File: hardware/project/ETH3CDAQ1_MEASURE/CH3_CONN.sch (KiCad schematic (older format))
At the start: 1 part, among them J1301 Conn_02x10_Odd_Even

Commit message: PCB layout
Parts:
- renumbered J1301 to J1001
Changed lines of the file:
@@
 AR Path="/5FDF6197/5FF0E84A" Ref="J?"  Part="1"
 AR Path="/5FE2FF08/5FF0E84A" Ref="J?"  Part="1"
-AR Path="/5FF09887/5FF0E84A" Ref="J1301"  Part="1"
-F 0 "J1301" H 5450 3667 50  0000 C CNN
+AR Path="/5FF09887/5FF0E84A" Ref="J1001"  Part="1"
+F 0 "J1001" H 5450 3667 50  0000 C CNN
 F 1 "Conn_02x10_Odd_Even" H 5450 3576 50  0000 C CNN
 F 2 "Connector_PinSocket_2.54mm:PinSocket_2x10_P2.54mm_Vertical" H 5400 3050 50  0001 C CNN
@@
 AR Path="/5FDF6197/5FF0E850" Ref="#PWR?"  Part="1"
 AR Path="/5FE2FF08/5FF0E850" Ref="#PWR?"  Part="1"
-AR Path="/5FF09887/5FF0E850" Ref="#PWR01302"  Part="1"
-F 0 "#PWR01302" H 5200 2500 50  0001 C CNN
+AR Path="/5FF09887/5FF0E850" Ref="#PWR01002"  Part="1"
+F 0 "#PWR01002" H 5200 2500 50  0001 C CNN
 F 1 "GND" V 5200 2600 50  0000 R CNN
 F 2 "" H 5200 2750 50  0001 C CNN
@@
 AR Path="/5FDF6197/5FF0E856" Ref="#PWR?"  Part="1"
 AR Path="/5FE2FF08/5FF0E856" Ref="#PWR?"  Part="1"
-AR Path="/5FF09887/5FF0E856" Ref="#PWR01303"  Part="1"
-F 0 "#PWR01303" H 5200 2600 50  0001 C CNN
+AR Path="/5FF09887/5FF0E856" Ref="#PWR01003"  Part="1"
+F 0 "#PWR01003" H 5200 2600 50  0001 C CNN
 F 1 "GND" V 5200 2700 50  0000 R CNN
 F 2 "" H 5200 2850 50  0001 C CNN
@@
 AR Path="/5FDF6197/5FF0E85C" Ref="#PWR?"  Part="1"
 AR Path="/5FE2FF08/5FF0E85C" Ref="#PWR?"  Part="1"
-AR Path="/5FF09887/5FF0E85C" Ref="#PWR01308"  Part="1"
-F 0 "#PWR01308" H 5700 2600 50  0001 C CNN
+AR Path="/5FF09887/5FF0E85C" Ref="#PWR01008"  Part="1"
+F 0 "#PWR01008" H 5700 2600 50  0001 C CNN
 F 1 "GND" V 5700 2700 50  0000 R CNN
 F 2 "" H 5700 2850 50  0001 C CNN
@@
 AR Path="/5FDF6197/5FF0E862" Ref="#PWR?"  Part="1"
 AR Path="/5FE2FF08/5FF0E862" Ref="#PWR?"  Part="1"
-AR Path="/5FF09887/5FF0E862" Ref="#PWR01301"  Part="1"
-F 0 "#PWR01301" H 5200 2400 50  0001 C CNN
+AR Path="/5FF09887/5FF0E862" Ref="#PWR01001"  Part="1"
+F 0 "#PWR01001" H 5200 2400 50  0001 C CNN
 F 1 "GND" V 5200 2500 50  0000 R CNN
 F 2 "" H 5200 2650 50  0001 C CNN
@@
 AR Path="/5FDF6197/5FF0E87C" Ref="#PWR?"  Part="1"
 AR Path="/5FE2FF08/5FF0E87C" Ref="#PWR?"  Part="1"
-AR Path="/5FF09887/5FF0E87C" Ref="#PWR01304"  Part="1"
-F 0 "#PWR01304" H 5200 3000 50  0001 C CNN
+AR Path="/5FF09887/5FF0E87C" Ref="#PWR01004"  Part="1"
+F 0 "#PWR01004" H 5200 3000 50  0001 C CNN
 F 1 "GND" V 5200 3100 50  0000 R CNN
 F 2 "" H 5200 3250 50  0001 C CNN
@@
 AR Path="/5FDF6197/5FF0E882" Ref="#PWR?"  Part="1"
 AR Path="/5FE2FF08/5FF0E882" Ref="#PWR?"  Part="1"
-AR Path="/5FF09887/5FF0E882" Ref="#PWR01309"  Part="1"
-F 0 "#PWR01309" H 5700 3000 50  0001 C CNN
+AR Path="/5FF09887/5FF0E882" Ref="#PWR01009"  Part="1"
+F 0 "#PWR01009" H 5700 3000 50  0001 C CNN
 F 1 "GND" V 5700 3100 50  0000 R CNN
 F 2 "" H 5700 3250 50  0001 C CNN
@@
 AR Path="/5FDF6197/5FF0E888" Ref="#PWR?"  Part="1"
 AR Path="/5FE2FF08/5FF0E888" Ref="#PWR?"  Part="1"
-AR Path="/5FF09887/5FF0E888" Ref="#PWR01305"  Part="1"
-F 0 "#PWR01305" H 5200 3200 50  0001 C CNN
+AR Path="/5FF09887/5FF0E888" Ref="#PWR01005"  Part="1"
+F 0 "#PWR01005" H 5200 3200 50  0001 C CNN
 F 1 "+3.3V" V 5200 3500 50  0000 L CNN
 F 2 "" H 5200 3350 50  0001 C CNN
@@
 AR Path="/5FDF6197/5FF0E88E" Ref="#PWR?"  Part="1"
 AR Path="/5FE2FF08/5FF0E88E" Ref="#PWR?"  Part="1"
-AR Path="/5FF09887/5FF0E88E" Ref="#PWR01310"  Part="1"
-F 0 "#PWR01310" H 5700 3200 50  0001 C CNN
+AR Path="/5FF09887/5FF0E88E" Ref="#PWR01010"  Part="1"
+F 0 "#PWR01010" H 5700 3200 50  0001 C CNN
 F 1 "+3.3V" V 5700 3500 50  0000 L CNN
 F 2 "" H 5700 3350 50  0001 C CNN
@@
 AR Path="/5FDF6197/5FF0E894" Ref="#PWR?"  Part="1"
 AR Path="/5FE2FF08/5FF0E894" Ref="#PWR?"  Part="1"
-AR Path="/5FF09887/5FF0E894" Ref="#PWR01306"  Part="1"
-F 0 "#PWR01306" H 5200 3300 50  0001 C CNN
+AR Path="/5FF09887/5FF0E894" Ref="#PWR01006"  Part="1"
+F 0 "#PWR01006" H 5200 3300 50  0001 C CNN
 F 1 "+9V" V 5200 3600 50  0000 L CNN
 F 2 "" H 5200 3450 50  0001 C CNN
@@
 AR Path="/5FDF6197/5FF0E89A" Ref="#PWR?"  Part="1"
 AR Path="/5FE2FF08/5FF0E89A" Ref="#PWR?"  Part="1"
-AR Path="/5FF09887/5FF0E89A" Ref="#PWR01311"  Part="1"
-F 0 "#PWR01311" H 5700 3300 50  0001 C CNN
+AR Path="/5FF09887/5FF0E89A" Ref="#PWR01011"  Part="1"
+F 0 "#PWR01011" H 5700 3300 50  0001 C CNN
 F 1 "+5V" V 5700 3600 50  0000 L CNN
 F 2 "" H 5700 3450 50  0001 C CNN
@@
 AR Path="/5FDF6197/5FF0E8A0" Ref="#PWR?"  Part="1"
 AR Path="/5FE2FF08/5FF0E8A0" Ref="#PWR?"  Part="1"
-AR Path="/5FF09887/5FF0E8A0" Ref="#PWR01307"  Part="1"
-F 0 "#PWR01307" H 5200 3400 50  0001 C CNN
+AR Path="/5FF09887/5FF0E8A0" Ref="#PWR01007"  Part="1"
+F 0 "#PWR01007" H 5200 3400 50  0001 C CNN
 F 1 "-18V" V 5200 3700 50  0000 L CNN
 F 2 "" H 5200 3550 50  0001 C CNN
@@
 AR Path="/5FDF6197/5FF0E8A6" Ref="#PWR?"  Part="1"
 AR Path="/5FE2FF08/5FF0E8A6" Ref="#PWR?"  Part="1"
-AR Path="/5FF09887/5FF0E8A6" Ref="#PWR01312"  Part="1"
-F 0 "#PWR01312" H 5700 3400 50  0001 C CNN
+AR Path="/5FF09887/5FF0E8A6" Ref="#PWR01012"  Part="1"
+F 0 "#PWR01012" H 5700 3400 50  0001 C CNN
 F 1 "+18V" V 5700 3700 50  0000 L CNN
 F 2 "" H 5700 3550 50  0001 C CNN

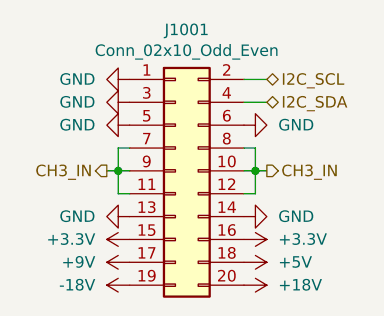
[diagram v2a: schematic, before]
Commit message: Started development of first current measurement module. Added CAN to the DAQ module.
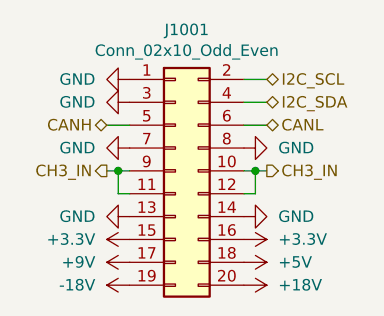
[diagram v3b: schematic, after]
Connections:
- net CH3_IN: no longer J1001.7 (Pin_7), J1001.8 (Pin_8)
- net GND: now also J1001.7 (Pin_7), J1001.8 (Pin_8); no longer J1001.5 (Pin_5), J1001.6 (Pin_6)
- new net CANH: J1001.5 (Pin_5)
- new net CANL: J1001.6 (Pin_6)
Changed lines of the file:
@@
 $Descr A4 11693 8268
 encoding utf-8
-Sheet 13 15
+Sheet 10 15
 Title ""
 Date ""
@@
 $Comp
 L power:GND #PWR?
-U 1 1 5FF0E850
-P 5200 2750
-AR Path="/5FDF6197/5FF0E850" Ref="#PWR?"  Part="1"
-AR Path="/5FE2FF08/5FF0E850" Ref="#PWR?"  Part="1"
-AR Path="/5FF09887/5FF0E850" Ref="#PWR01002"  Part="1"
-F 0 "#PWR01002" H 5200 2500 50  0001 C CNN
-F 1 "GND" V 5200 2600 50  0000 R CNN
-F 2 "" H 5200 2750 50  0001 C CNN
-F 3 "" H 5200 2750 50  0001 C CNN
-	1    5200 2750
-	0    1    1    0
-$EndComp
-$Comp
-L power:GND #PWR?
-U 1 1 5FF0E856
-P 5200 2850
-AR Path="/5FDF6197/5FF0E856" Ref="#PWR?"  Part="1"
-AR Path="/5FE2FF08/5FF0E856" Ref="#PWR?"  Part="1"
-AR Path="/5FF09887/5FF0E856" Ref="#PWR01003"  Part="1"
-F 0 "#PWR01003" H 5200 2600 50  0001 C CNN
-F 1 "GND" V 5200 2700 50  0000 R CNN
-F 2 "" H 5200 2850 50  0001 C CNN
-F 3 "" H 5200 2850 50  0001 C CNN
-	1    5200 2850
-	0    1    1    0
-$EndComp
-$Comp
-L power:GND #PWR?
-U 1 1 5FF0E85C
-P 5700 2850
-AR Path="/5FDF6197/5FF0E85C" Ref="#PWR?"  Part="1"
-AR Path="/5FE2FF08/5FF0E85C" Ref="#PWR?"  Part="1"
-AR Path="/5FF09887/5FF0E85C" Ref="#PWR01008"  Part="1"
-F 0 "#PWR01008" H 5700 2600 50  0001 C CNN
-F 1 "GND" V 5700 2700 50  0000 R CNN
-F 2 "" H 5700 2850 50  0001 C CNN
-F 3 "" H 5700 2850 50  0001 C CNN
-	1    5700 2850
-	0    -1   -1   0
-$EndComp
-$Comp
-L power:GND #PWR?
 U 1 1 5FF0E862
 P 5200 2650
@@
 	5700 2650 5800 2650
 Wire Wire Line
-	5700 2950 5750 2950
-Wire Wire Line
-	5750 2950 5750 3050
-Wire Wire Line
 	5750 3150 5700 3150
 Wire Wire Line
@@
 Wire Wire Line
 	5750 3050 5750 3150
-Wire Wire Line
-	5200 2950 5150 2950
-Wire Wire Line
-	5150 2950 5150 3050
 Wire Wire Line
 	5150 3150 5200 3150
@@
 	0    1    1    0
 $EndComp
+$Comp
+L power:GND #PWR?
+U 1 1 5FE5D062
+P 5200 2750
+AR Path="/5FDF6197/5FE5D062" Ref="#PWR?"  Part="1"
+AR Path="/5FE2FF08/5FE5D062" Ref="#PWR?"  Part="1"
+AR Path="/5FF09887/5FE5D062" Ref="#PWR01002"  Part="1"
+F 0 "#PWR01002" H 5200 2500 50  0001 C CNN
+F 1 "GND" V 5200 2600 50  0000 R CNN
+F 2 "" H 5200 2750 50  0001 C CNN
+F 3 "" H 5200 2750 50  0001 C CNN
+	1    5200 2750
+	0    1    1    0
+$EndComp
+$Comp
+L power:GND #PWR?
+U 1 1 5FE60DCD
+P 5200 2950
+AR Path="/5FDF6197/5FE60DCD" Ref="#PWR?"  Part="1"
+AR Path="/5FE2FF08/5FE60DCD" Ref="#PWR?"  Part="1"
+AR Path="/5FF09887/5FE60DCD" Ref="#PWR01003"  Part="1"
+F 0 "#PWR01003" H 5200 2700 50  0001 C CNN
+F 1 "GND" V 5200 2800 50  0000 R CNN
+F 2 "" H 5200 2950 50  0001 C CNN
+F 3 "" H 5200 2950 50  0001 C CNN
+	1    5200 2950
+	0    1    1    0
+$EndComp
+$Comp
+L power:GND #PWR?
+U 1 1 5FE61008
+P 5700 2950
+AR Path="/5FDF6197/5FE61008" Ref="#PWR?"  Part="1"
+AR Path="/5FE2FF08/5FE61008" Ref="#PWR?"  Part="1"
+AR Path="/5FF09887/5FE61008" Ref="#PWR01008"  Part="1"
+F 0 "#PWR01008" H 5700 2700 50  0001 C CNN
+F 1 "GND" V 5700 2800 50  0000 R CNN
+F 2 "" H 5700 2950 50  0001 C CNN
+F 3 "" H 5700 2950 50  0001 C CNN
+	1    5700 2950
+	0    -1   -1   0
+$EndComp
+Wire Wire Line
+	5700 2850 5800 2850
+Wire Wire Line
+	5200 2850 5100 2850
+Text HLabel 5100 2850 0    50   BiDi ~ 0
+CANH
+Text HLabel 5800 2850 2    50   BiDi ~ 0
+CANL
 $EndSCHEMATC
